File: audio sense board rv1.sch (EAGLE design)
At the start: 31 parts, among them IC2 TSOP38238, J1 PJRAN1X1U01X, J4 PJRAN1X1U01X, Q1 2N3904, Q2 2N3904

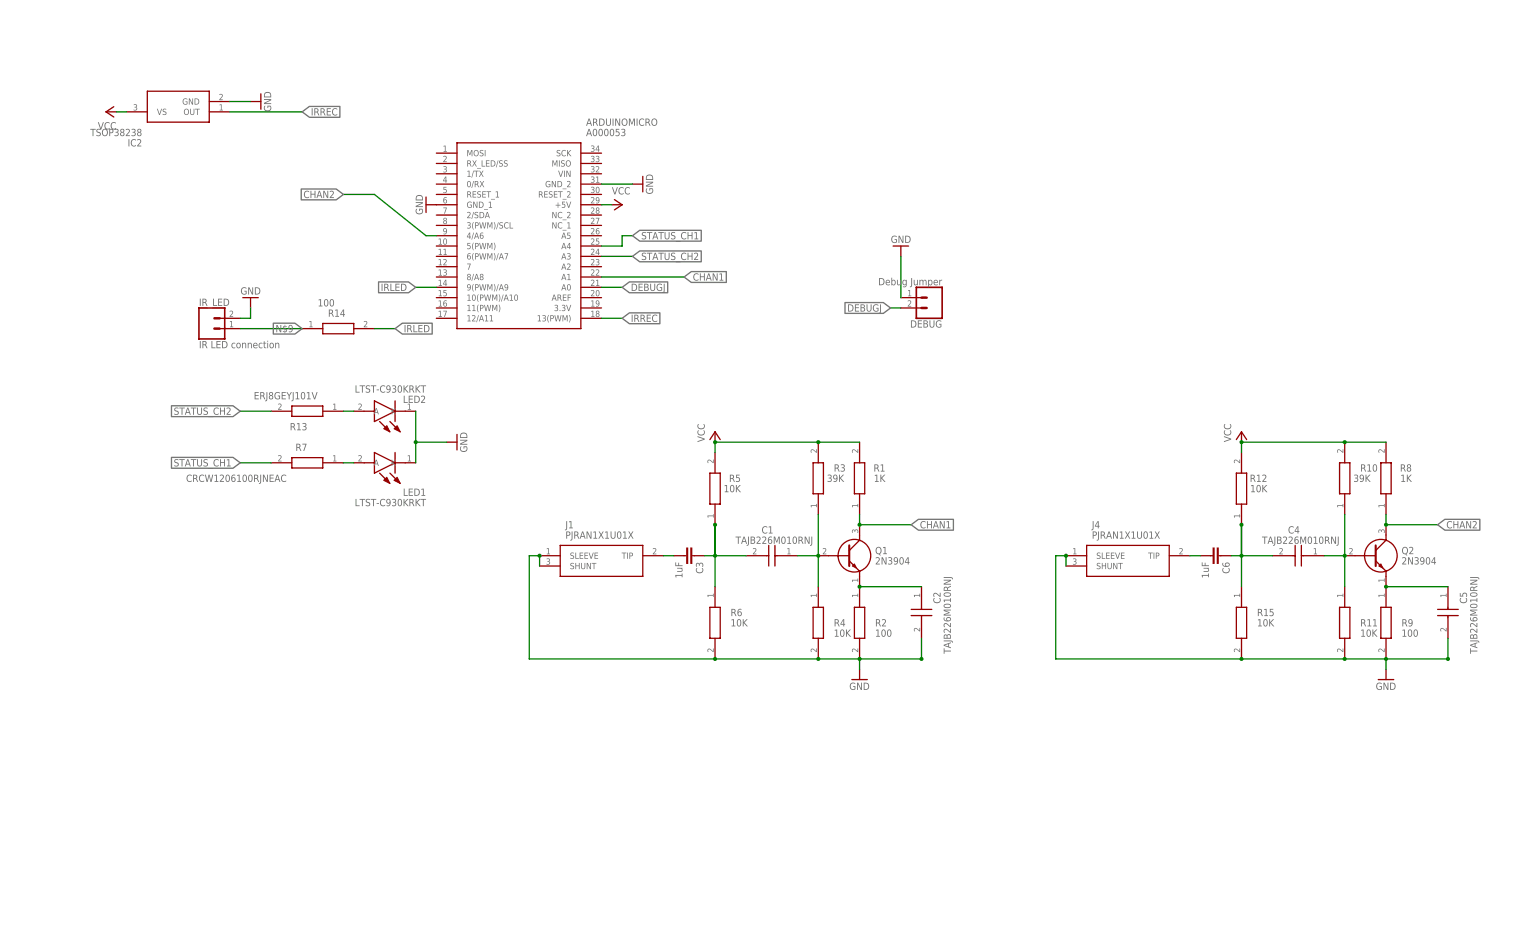
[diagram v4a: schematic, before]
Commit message: add transformers
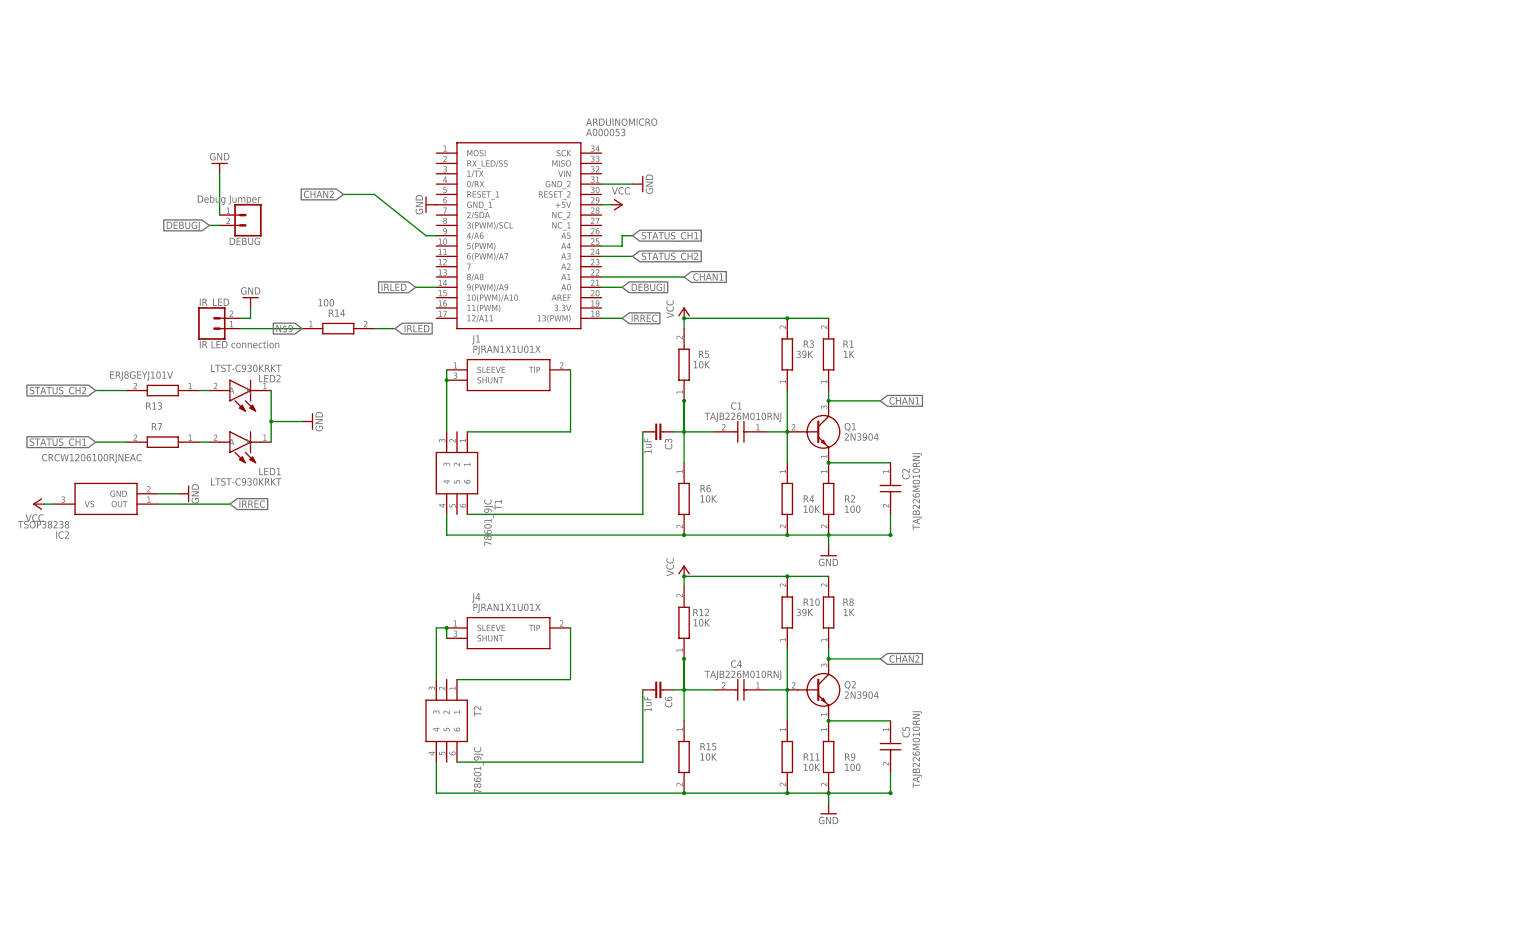
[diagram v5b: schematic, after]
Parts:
- added T1, T2: 78601_9JC, Samac Populated:78601_9JC
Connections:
- removed net N$16: C6.2, J4.TIP
- new net N$10: C6.2, T2.6
- new net N$11: J1.SHUNT, J1.SLEEVE, T1.3
- new net N$13: C3.2, T1.6
- new net N$5: J4.SHUNT, J4.SLEEVE, T2.3
- new net N$8: J4.TIP, T2.1
- net GND: now also T1.4, T2.4; no longer J1.SHUNT, J1.SLEEVE, J4.SHUNT, J4.SLEEVE
- net N$6: now also T1.1; no longer C3.2
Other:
- moved on the sheet: C1, C2, C3, C4, C5, C6, DEBUG, IC2, J1, J4, LED1, LED2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

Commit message: correcting issue - voltage divider in wrong location in both channels
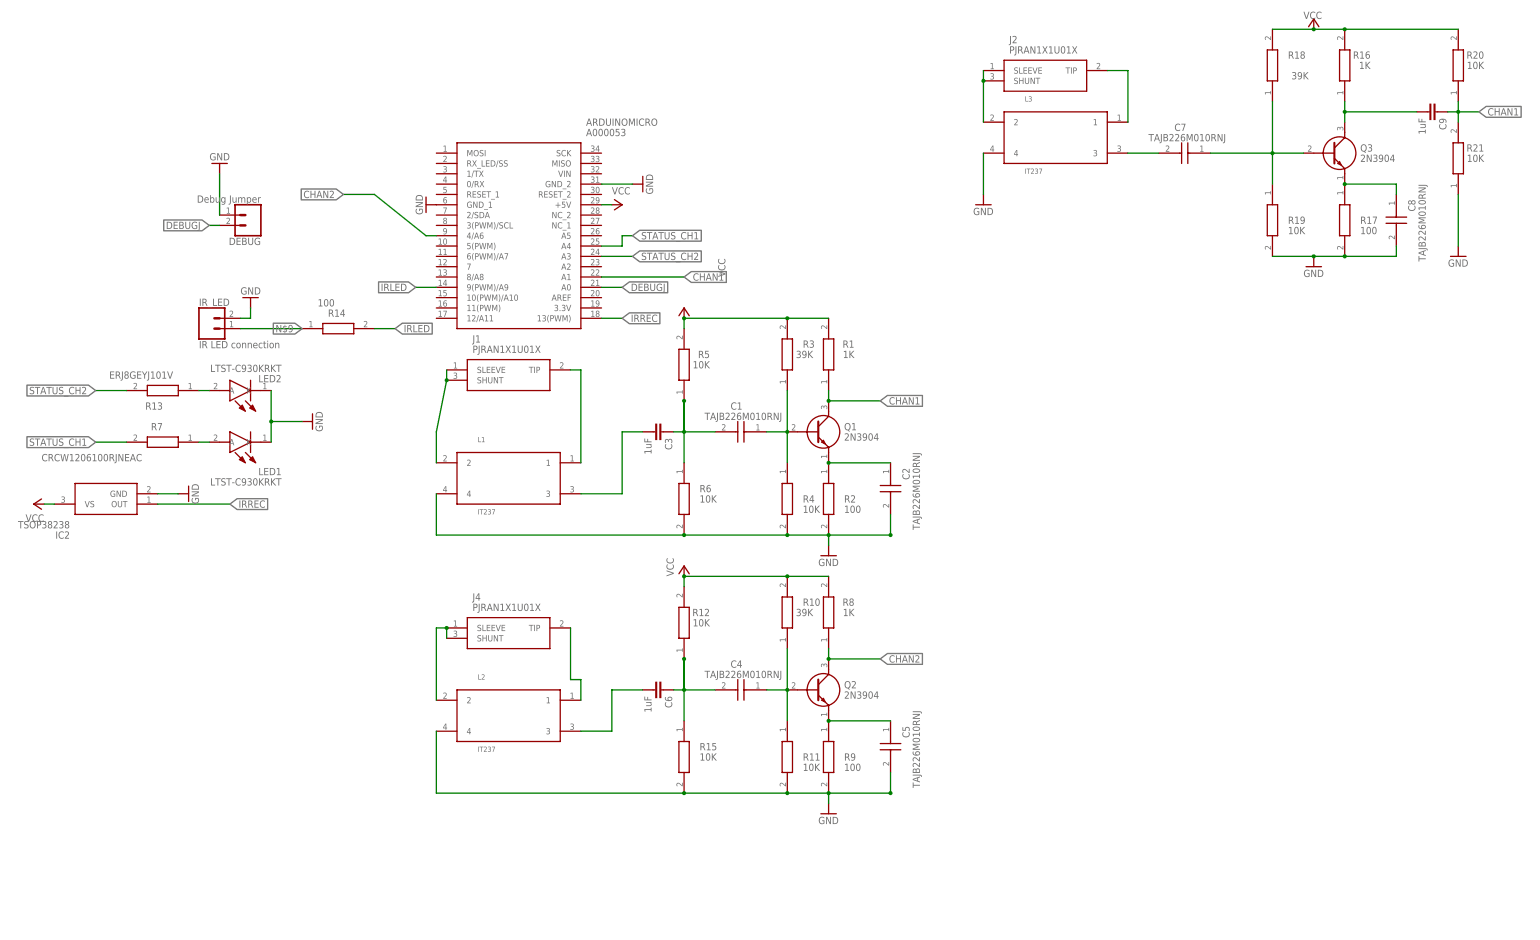
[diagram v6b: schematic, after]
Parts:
- removed T1, T2: 78601_9JC, Samac Populated:78601_9JC
- added C7, C8: TAJB226M010RNJ, Samac Populated:TAJB226M010RNJ
- added C9: 1uF, SparkFun-Capacitors:22PF-PTH-2.54MM-200V-5%
- added J2: PJRAN1X1U01X, Samac Populated:PJRAN1X1U01X
- added L1, L2, L3: IT237, My Library:IT237
- added Q3: 2N3904, Samac Populated:2N3904
- added R16: 1K, Samac Populated:ERJ-8GEYJ102V
- added R17: 100, Samac Populated:ERJ8GEYJ101V
- added R18: 39K, Samac Populated:ERJ8GEYJ101V
- added R19, R20, R21: 10K, Samac Populated:ERJ8GEYJ101V
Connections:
- new net N$12: J2.SHUNT, J2.SLEEVE, L3.2
- new net N$15: J2.TIP, L3.1
- new net N$16: C7.+, Q3.B, R18.1, R19.1
- new net N$17: C7.-, L3.3
- new net N$20: C8.+, Q3.E, R17.1
- new net N$21: C9.2, Q3.C, R16.1
- net CHAN1: now also C9.1, R20.1, R21.2
- net GND: now also C8.-, L1.4, L2.4, L3.4, R17.2, R19.2, R21.1; no longer T1.4, T2.4
- net N$10: now also C3.2, L1.3; no longer C6.2, T2.6
- net N$11: now also L1.2; no longer T1.3
- net N$13: now also C6.2, L2.3; no longer C3.2, T1.6
- net N$5: now also L2.2; no longer T2.3
- net N$6: now also L1.1; no longer T1.1
- net N$8: now also L2.1; no longer T2.1
- net VCC: now also R16.2, R18.2, R20.2

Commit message: remove improper components, rework circuit
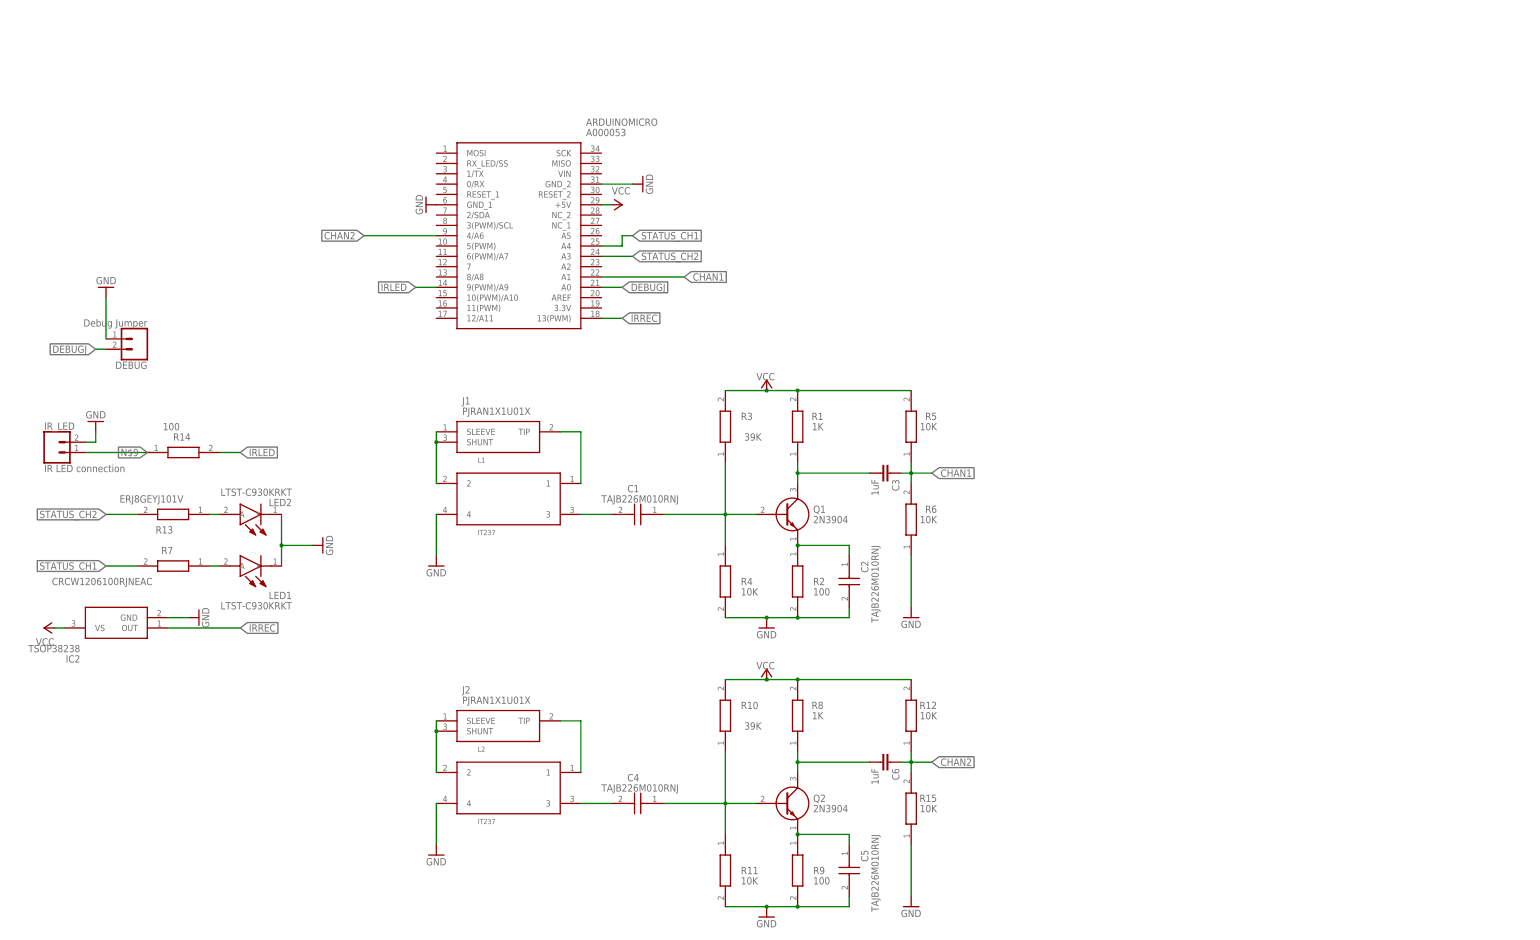
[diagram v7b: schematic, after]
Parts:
- removed C7, C8: TAJB226M010RNJ, Samac Populated:TAJB226M010RNJ
- removed C9: 1uF, SparkFun-Capacitors:22PF-PTH-2.54MM-200V-5%
- removed J4: PJRAN1X1U01X, Samac Populated:PJRAN1X1U01X
- removed L3: IT237, My Library:IT237
- removed Q3: 2N3904, Samac Populated:2N3904
- removed R16: 1K, Samac Populated:ERJ-8GEYJ102V
- removed R17: 100, Samac Populated:ERJ8GEYJ101V
- removed R18: 39K, Samac Populated:ERJ8GEYJ101V
- removed R19, R20, R21: 10K, Samac Populated:ERJ8GEYJ101V
- R8: device Samac Populated:ERJ8GEYJ101V -> Samac Populated:ERJ-8GEYJ102V
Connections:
- removed net N$10: C3.2, L1.3
- removed net N$12 (its old number): J2.SHUNT, J2.SLEEVE, L3.2
- removed net N$13: C6.2, L2.3
- removed net N$15 (its old number): J2.TIP, L3.1
- removed net N$16 (its old number): C7.+, Q3.B, R18.1, R19.1
- removed net N$18: C4.-, C6.1, R12.1, R15.1
- removed net N$20 (its old number): C8.+, Q3.E, R17.1
- removed net N$7 (its old number): C1.-, C3.1, R5.1, R6.1
- new net N$1: J2.SHUNT, J2.SLEEVE, L2.2
- new net N$3: J2.TIP, L2.1
- net CHAN1: now also C3.1, R5.1, R6.2; no longer C9.1, Q1.C, R1.1, R20.1, R21.2
- net CHAN2: now also C6.1, R12.1, R15.2; no longer Q2.C, R8.1
- net GND: now also R15.1, R6.1; no longer C8.-, L3.4, R15.2, R17.2, R19.2, R21.1, R6.2
- net N$17: now also C1.-, L1.3; no longer C7.-, L3.3
- net N$21: now also C3.2, Q1.C, R1.1; no longer C9.2, Q3.C, R16.1
- net N$5: now also C4.-, L2.3; no longer J4.SHUNT, J4.SLEEVE, L2.2
- net N$8: now also C6.2, Q2.C, R8.1; no longer J4.TIP, L2.1
- net VCC: no longer R16.2, R18.2, R20.2
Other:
- moved on the sheet: C1, C2, C3, C4, C5, C6, DEBUG, IC2, IR_LED, J1, J2, L1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
